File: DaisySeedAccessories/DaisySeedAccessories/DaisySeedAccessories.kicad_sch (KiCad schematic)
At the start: 0 parts

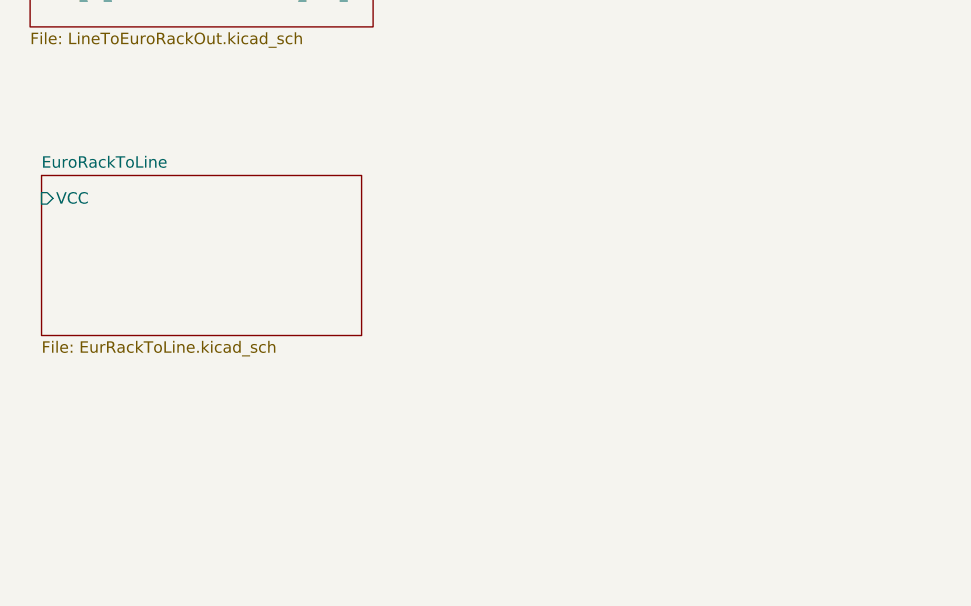
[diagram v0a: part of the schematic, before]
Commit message: commit before simplifyting the board further
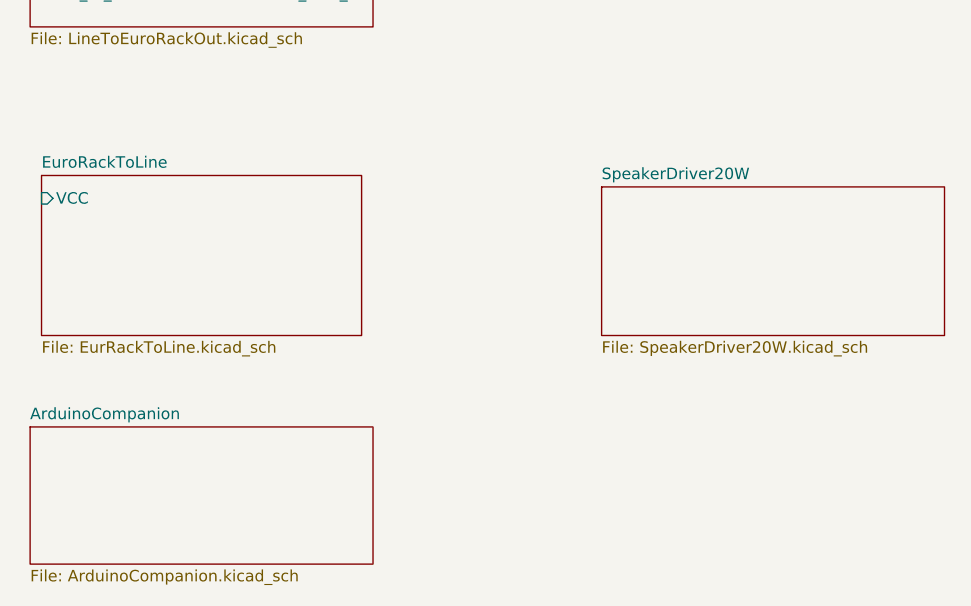
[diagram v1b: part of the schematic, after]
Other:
- added sheet ArduinoCompanion (ArduinoCompanion.kicad_sch)
- added sheet SpeakerDriver20W (SpeakerDriver20W.kicad_sch)
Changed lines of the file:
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@@
 (kicad_sch (version 20230121) (generator eeschema)
   (paper "A4")
+  (sheet (at 154.94 96.52) (size 38.1 16.51) (fields_autoplaced)
+    (stroke (width 0.1524) (type solid))
+    (fill (color 0 0 0 0.0000))
+    (property "Sheetname" "SpeakerDriver20W" (at 154.94 95.8084 0)
+      (effects (font (size 1.27 1.27)) (justify left bottom))
+    )
+    (property "Sheetfile" "SpeakerDriver20W.kicad_sch" (at 154.94 113.6146 0)
+      (effects (font (size 1.27 1.27)) (justify left top))
+    )
+    (instances
+      (project "DaisySeedAccessories"
+        (path "/f4e212fd-fab8-40de-a317-91335511a529" (page "7"))
+      )
+    )
+  )
   (sheet (at 91.44 64.77) (size 38.1 13.97) (fields_autoplaced)
     (stroke (width 0.1524) (type solid))
@@
       )
     )
+  )
+  (sheet (at 91.44 123.19) (size 38.1 15.24) (fields_autoplaced)
+    (stroke (width 0.1524) (type solid))
+    (fill (color 0 0 0 0.0000))
+    (property "Sheetname" "ArduinoCompanion" (at 91.44 122.4784 0)
+      (effects (font (size 1.27 1.27)) (justify left bottom))
+    )
+    (property "Sheetfile" "ArduinoCompanion.kicad_sch" (at 91.44 139.0146 0)
+      (effects (font (size 1.27 1.27)) (justify left top))
+    )
+    (instances
+      (project "DaisySeedAccessories"
+        (path "/f4e212fd-fab8-40de-a317-91335511a529" (page "8"))
+      )
+    )

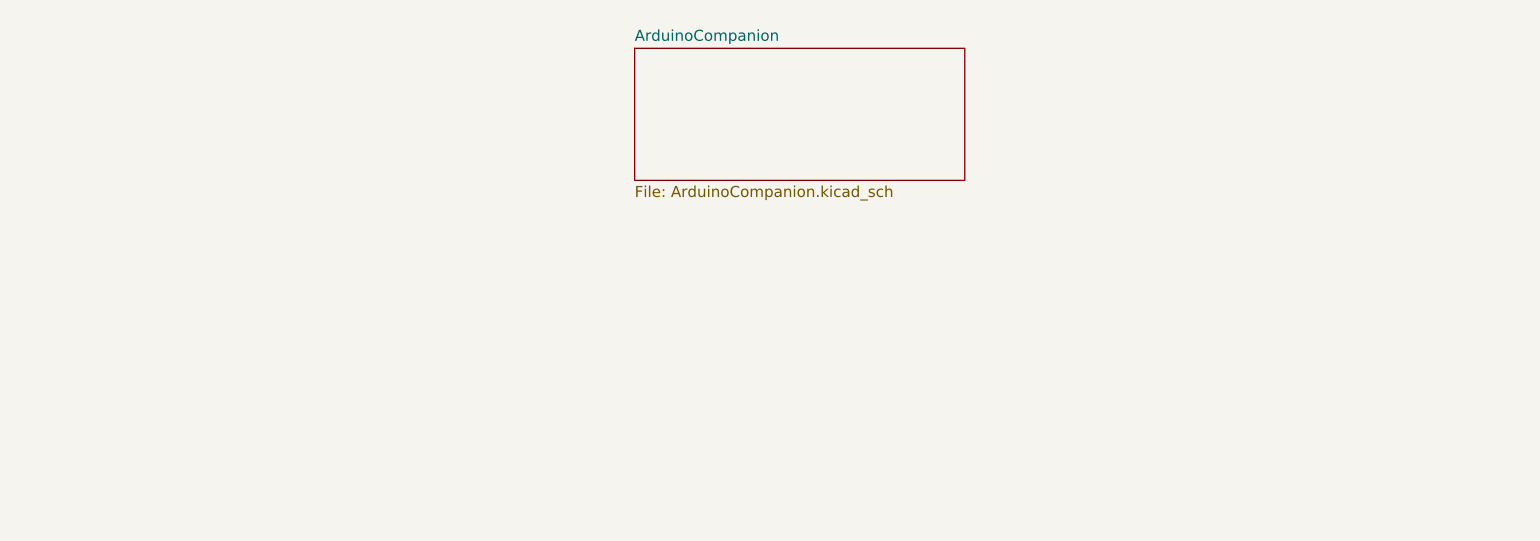
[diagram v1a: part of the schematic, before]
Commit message: simplified design, rely on external boards more to cover those cases
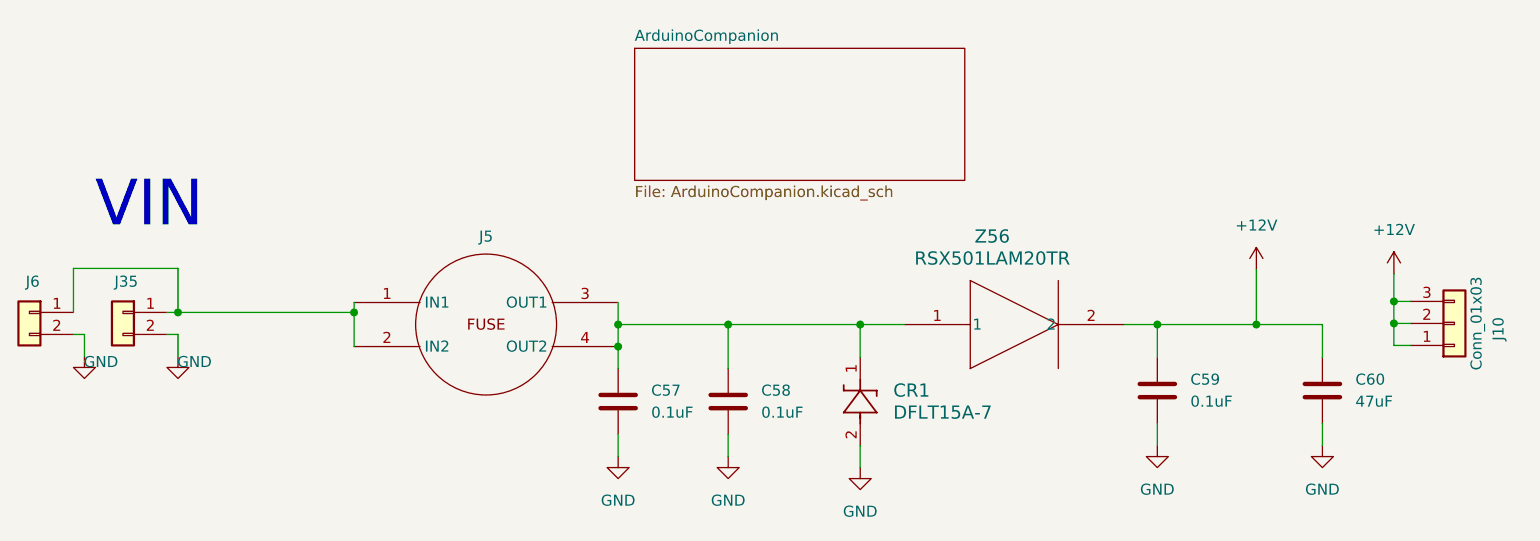
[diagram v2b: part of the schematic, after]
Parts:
- added C57, C58, C59: 0.1uF, Capacitor_SMD:C_0402_1005Metric, symbol Device:C
- added C60: 47uF, Capacitor_SMD:C_0805_2012Metric, symbol Device:C
- added CR1: DFLT15A-7, ZDO_POWERDI123_DIO, symbol 2023-10-02_00-55-35:DFLT15A-7
- added J10: Conn_01x03, Ultralibrarian:PinHeader_1x03_P2.54mm_Vertical_Female, symbol 4ms_Connector:Conn_01x03
- added J35, J6: Conn_01x02, 1x2FemaleVertical:PinHeader_1x02_P2.54mm_VerticalFemale, symbol 4ms_Connector:Conn_01x02
- added J5: ~, Ultralibrarian:BladeFuseHolder, symbol Ultralibrarian_modified_symbols:BladeFuseHolder
- added Z56: RSX501LAM20TR, DIO_RB050LAM_ROM, symbol 2023-10-01_23-34-18:RSX501LAM20TR
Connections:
- new net: J35.1 (Pin_1), J5.1 (IN1), J5.2 (IN2), J6.1 (Pin_1)
- new net: C57.1, C58.1, CR1.1, J5.3 (OUT1), J5.4 (OUT2), Z56.1
- new net +12V: C59.1, C60.1, J10.1 (Pin_1), J10.2 (Pin_2), J10.3 (Pin_3), Z56.2
- new net GND: C57.2, C58.2, C59.2, C60.2, CR1.2, J35.2 (Pin_2), J6.2 (Pin_2)
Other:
- note added: "VIN"

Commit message: periodic update
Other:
- added sheet 12V_To_5V (12V_To_5V.kicad_sch)
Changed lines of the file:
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@@
+    )
+  )
+  (sheet (at 215.9 82.55) (size 39.37 20.32) (fields_autoplaced)
+    (stroke (width 0.1524) (type solid))
+    (fill (color 0 0 0 0.0000))
+    (property "Sheetname" "12V_To_5V" (at 215.9 81.8384 0)
+      (effects (font (size 1.27 1.27)) (justify left bottom))
+    )
+    (property "Sheetfile" "12V_To_5V.kicad_sch" (at 215.9 103.4546 0)
+      (effects (font (size 1.27 1.27)) (justify left top))
+    )
+    (instances
+      (project "DaisySeedAccessories"
+        (path "/f4e212fd-fab8-40de-a317-91335511a529" (page "9"))
+      )
     )
   )
